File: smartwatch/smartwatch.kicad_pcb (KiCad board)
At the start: 4 copper layers, 40.1 x 29.7 mm, 35 parts, among them J1 BAT_CON, J2 DC_CON, J3 PROG_INT, J4 SM13B-GHS-TB, SW1 SW_Push, U1 ESP32-WROVER-E, U2 MCP73831-5-OT, U3 MPU-6050, U4 TLV1117-33

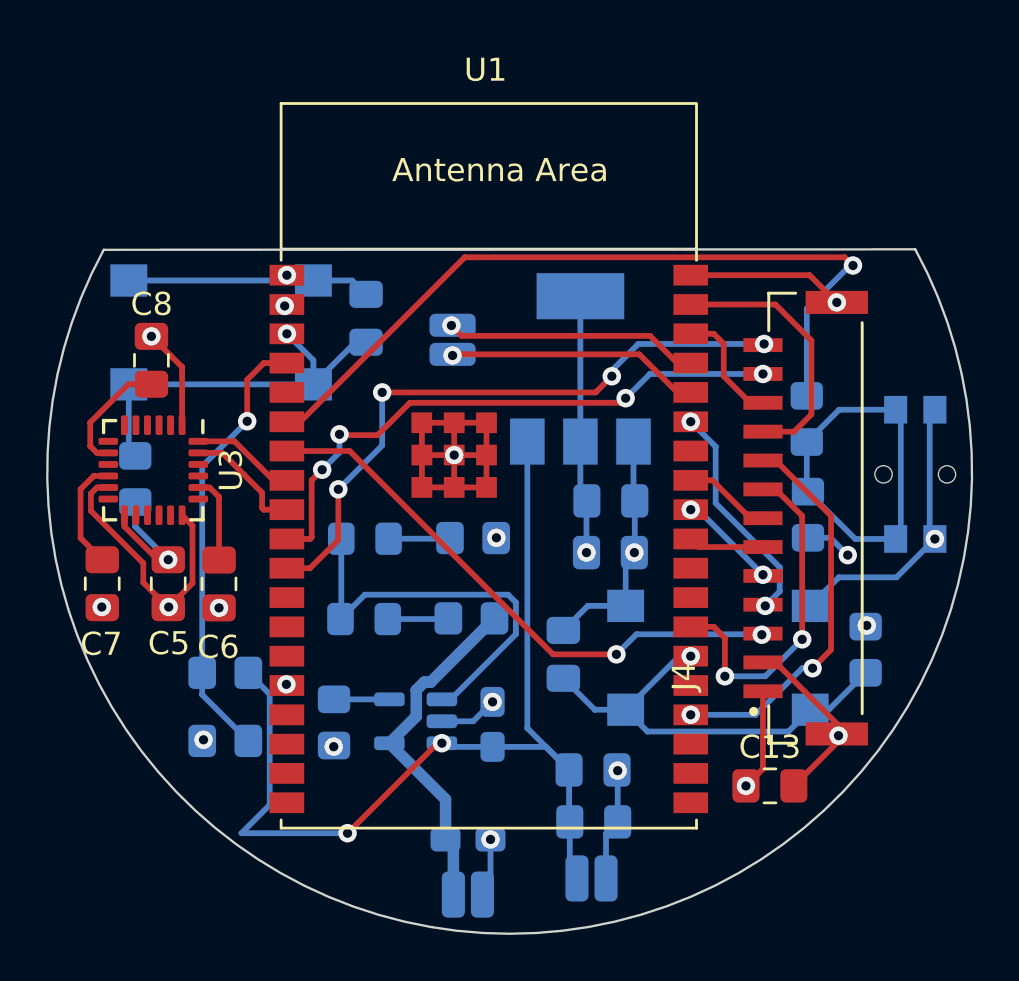
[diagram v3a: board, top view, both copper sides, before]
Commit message: added connectors for all and reroute
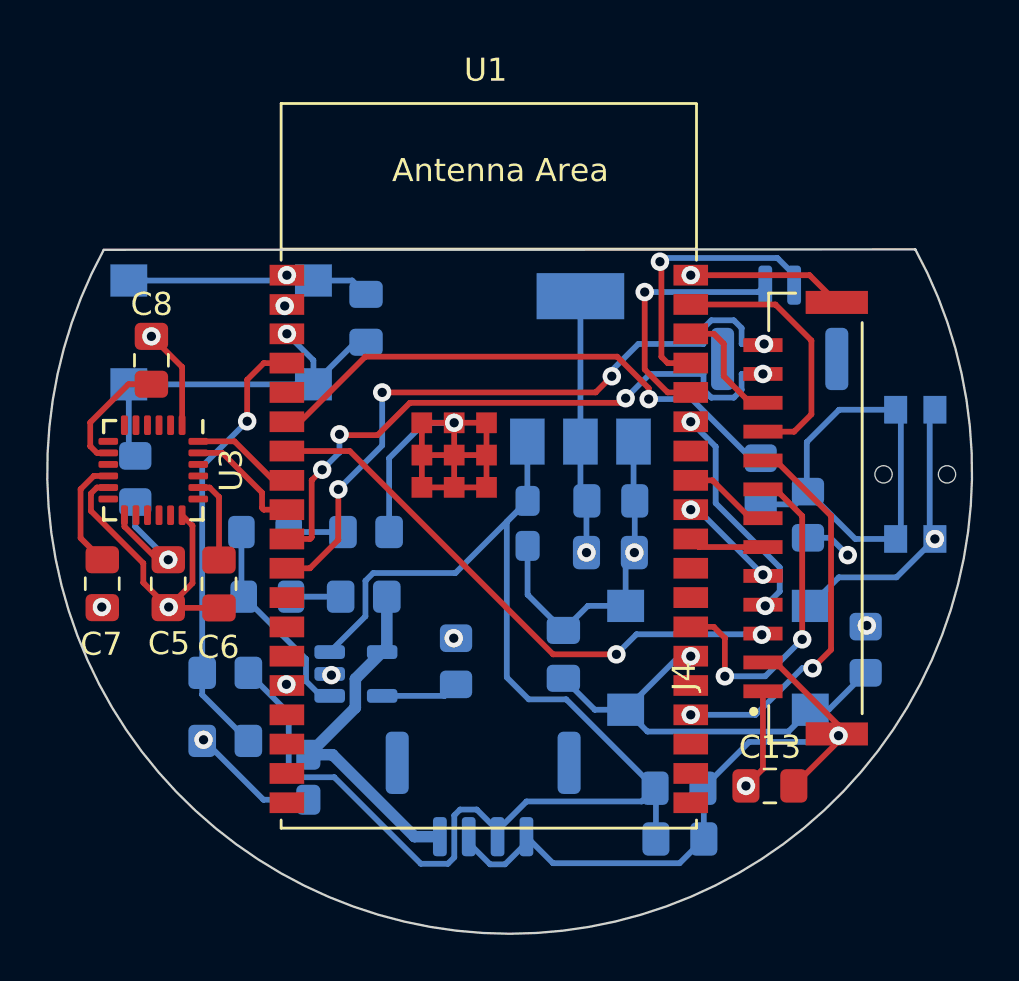
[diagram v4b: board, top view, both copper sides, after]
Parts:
- removed J1: BAT_CON, Connector_Wire_SMD:Wire_Pad_1x02
- removed J2: DC_CON, Connector_Wire_SMD:Wire_Pad_1x02
- removed J3: PROG_INT, Connector_Wire_SMD:Wire_Pad_1x02
- added J5: BAT_CON/DC_CON, Connector_JST:JST_GH_SM04B-GHS-TB_1x04-1MP_P1.25mm_Horizontal, B.Cu at (44.4, 56.5)
- added J6: PROG_INT, Connector_JST:JST_GH_SM02B-GHS-TB_1x02-1MP_P1.25mm_Horizontal, B.Cu at (57.2, 36.2)
- moved C11 8.84 mm to (46.3, 44.7), turned to -90 degrees
- moved C12 7.43 mm to (36.8, 55.7), turned to -90 degrees
- moved R1 5.91 mm to (43.2, 50.7), turned to 90 degrees
- moved R2 4.76 mm to (39.2, 47.9)
- moved R3 4.64 mm to (39.3, 45.1)
- moved GREEN1 4.34 mm to (34.9, 45.1)
- moved RED1 4.30 mm to (35.0, 47.9)
- moved C2 3.81 mm to (52.9, 56.2)
- moved C1 3.81 mm to (52.9, 58.4)
- moved R4 3.36 mm to (56.4, 42.9)
- moved U2 3.30 mm to (38.9, 51.2), turned to 0 degrees
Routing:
- net DC_GND: track 92.9 -> 122.9 mm, vias 17 -> 13
- net BAT_VDD: track 44.0 -> 59.4 mm, vias 2 -> 0
- net BTN_INP: track 34.2 -> 23.8 mm
- net MCP_1: track 17.4 -> 8.91 mm
- net Net-(R4-Pad1): track 17.0 -> 19.3 mm
- net TOUCH_RST: track 27.6 -> 29.2 mm
- net TOUCH_IRQ: track 25.5 -> 27.2 mm
- net TX: track 11.1 -> 12.2 mm
- net Net-(U2-PROG): track 2.40 -> 3.41 mm
